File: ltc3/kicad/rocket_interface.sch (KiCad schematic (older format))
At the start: 60 parts, among them IC1 TLP3542, J601 RJ45, K601 RELAY_1C, K602 RELAY_1C, P601 BATT-IN, P602 CONN_01x02, P603 UMBILICAL, Q601 PMV45EN, Q602 PMV45EN, SW601 SPST_switch, U602 CD74HC14, U603 SN65220DBV, U604 741G08

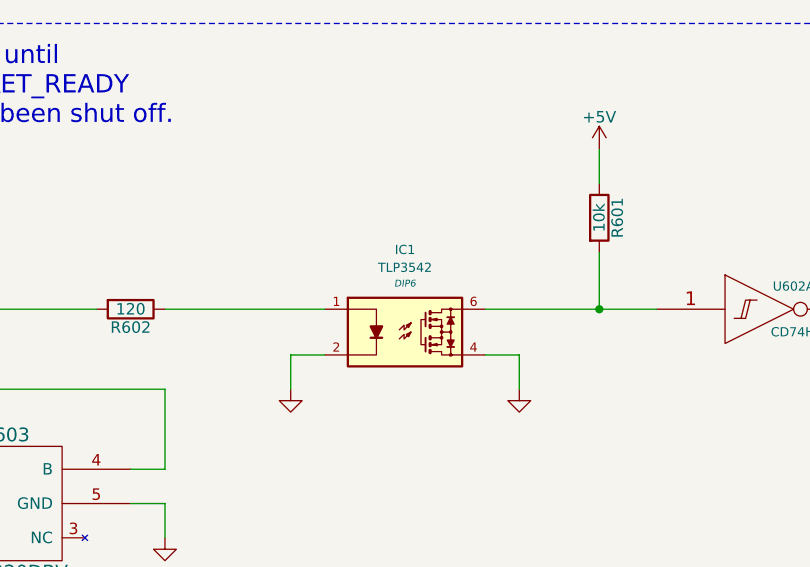
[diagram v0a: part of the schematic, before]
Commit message: Assigned more footprints, created PSOP-6 and PTN78020W.
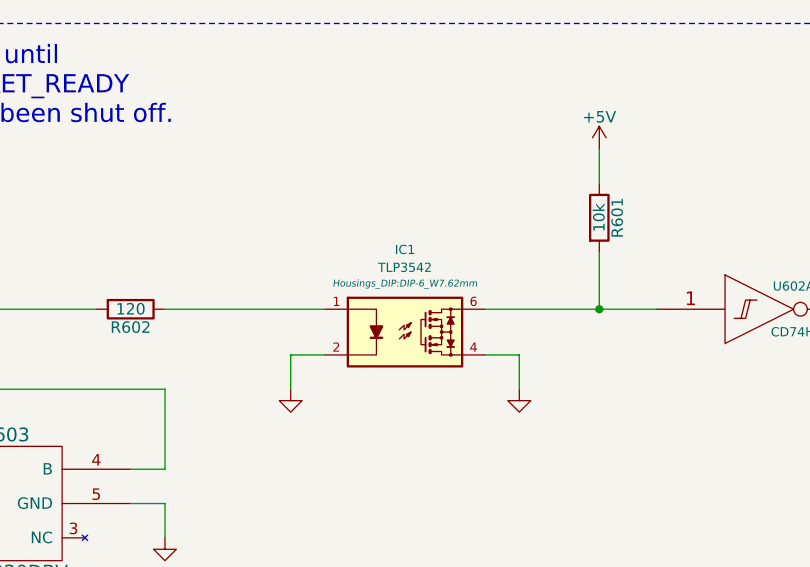
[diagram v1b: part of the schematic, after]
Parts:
- IC1: footprint DIP6 -> Housings_DIP:DIP-6_W7.62mm
- U602: footprint (none) -> Housings_SSOP:TSSOP-14_4.4x5mm_Pitch0.65mm
- U603: footprint (none) -> LTC3:PSOP-6
- U604: footprint (none) -> TO_SOT_Packages_SMD:SOT-353

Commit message: LTC3: Cosmetic changes; reference designator updates; etc.
1. Renamed "PHNTM*" reference designators to something more
   conventional and descriptive (e.g., "PHNTM*" to "BT*" for off-board
   batteries).
2. Cosmetic changes to battery management and BeagleBone schematics
   (normalizing text notes style, etc.).
3. Incremental progress on footprint assignment.
4. Imported netlist into PCB layout editor, just for grins.
   Everything fits into a 250x135mm board.  Only $260 for an OSH Park run!
   There may be some opportunities for improvement...
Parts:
- SW601: footprint (none) -> Oddities:Dummy_Empty
- W20, W21, W22, W23, W24, W25, W26, W27: footprint (none) -> Measurement_Points:Test_Point_2Pads
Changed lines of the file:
@@
 F 0 "SW601" H 14350 7050 60  0000 C CNN
 F 1 "SPST_switch" H 14370 6830 60  0001 C CNN
-F 2 "" H 14370 6950 60  0001 C CNN
+F 2 "Oddities:Dummy_Empty" H 14370 6950 60  0001 C CNN
 F 3 "" H 14370 6950 60  0000 C CNN
 F 4 "Ign. Arm" H 14350 6800 60  0000 C CNN "Note"
@@
 F 0 "W20" V 1404 2408 50  0000 L CNN
 F 1 "0/5V" V 1496 2408 50  0000 L CNN
-F 2 "" H 1450 2350 50  0001 C CNN
+F 2 "Measurement_Points:Test_Point_2Pads" H 1450 2350 50  0001 C CNN
 F 3 "" H 1450 2350 50  0000 C CNN
 	1    1450 2350
@@
 F 0 "W26" H 14750 1400 50  0000 C CNN
 F 1 "14.8-16.8V" H 14750 1500 50  0000 C CNN
-F 2 "" H 14750 1300 50  0001 C CNN
+F 2 "Measurement_Points:Test_Point_2Pads" H 14750 1300 50  0001 C CNN
 F 3 "" H 14750 1300 50  0000 C CNN
 	1    14750 1300
@@
 F 0 "W22" V 7350 3950 50  0000 L CNN
 F 1 "0/5V" V 7450 3850 50  0000 L CNN
-F 2 "" H 7400 4100 50  0001 C CNN
+F 2 "Measurement_Points:Test_Point_2Pads" H 7400 4100 50  0001 C CNN
 F 3 "" H 7400 4100 50  0000 C CNN
 	1    7400 4100
@@
 F 0 "W23" V 7504 4158 50  0000 L CNN
 F 1 "0/5V" V 7596 4158 50  0000 L CNN
-F 2 "" H 7550 4100 50  0001 C CNN
+F 2 "Measurement_Points:Test_Point_2Pads" H 7550 4100 50  0001 C CNN
 F 3 "" H 7550 4100 50  0000 C CNN
 	1    7550 4100
@@
 F 0 "W25" V 11150 3900 50  0000 L CNN
 F 1 "0/5V" V 11250 3850 50  0000 L CNN
-F 2 "" H 11200 4100 50  0001 C CNN
+F 2 "Measurement_Points:Test_Point_2Pads" H 11200 4100 50  0001 C CNN
 F 3 "" H 11200 4100 50  0000 C CNN
 	1    11200 4100
@@
 F 0 "W24" V 10354 8258 50  0000 L CNN
 F 1 "0/3.3V" V 10446 8258 50  0000 L CNN
-F 2 "" H 10400 8200 50  0001 C CNN
+F 2 "Measurement_Points:Test_Point_2Pads" H 10400 8200 50  0001 C CNN
 F 3 "" H 10400 8200 50  0000 C CNN
 	1    10400 8200
@@
 F 0 "W21" V 3104 4058 50  0000 L CNN
 F 1 "0/5V" V 3196 4058 50  0000 L CNN
-F 2 "" H 3150 4000 50  0001 C CNN
+F 2 "Measurement_Points:Test_Point_2Pads" H 3150 4000 50  0001 C CNN
 F 3 "" H 3150 4000 50  0000 C CNN
 	1    3150 4000
@@
 F 0 "W27" V 15004 8358 50  0000 L CNN
 F 1 "0/14.8-16.8V" V 15096 8358 50  0000 L CNN
-F 2 "" H 15050 8300 50  0001 C CNN
+F 2 "Measurement_Points:Test_Point_2Pads" H 15050 8300 50  0001 C CNN
 F 3 "" H 15050 8300 50  0000 C CNN
 	1    15050 8300

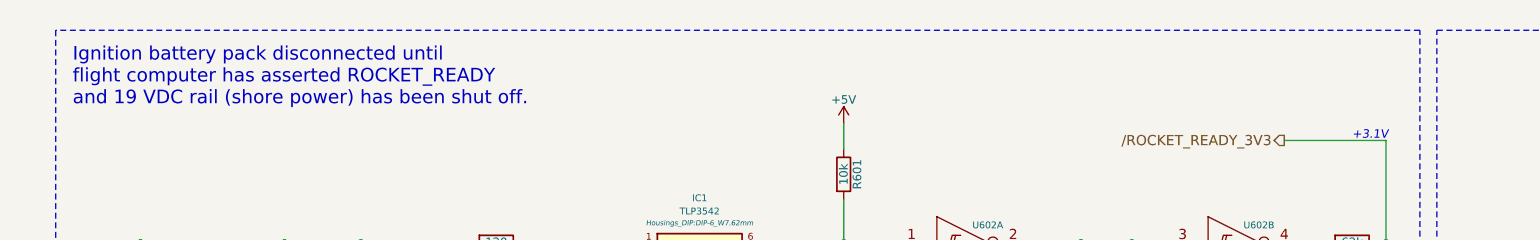
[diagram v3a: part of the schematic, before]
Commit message: Minor adjustment to BB cape footprint; more footprint assignments.
NB: "Valve" footprints are placeholder for components not yet
assigned.
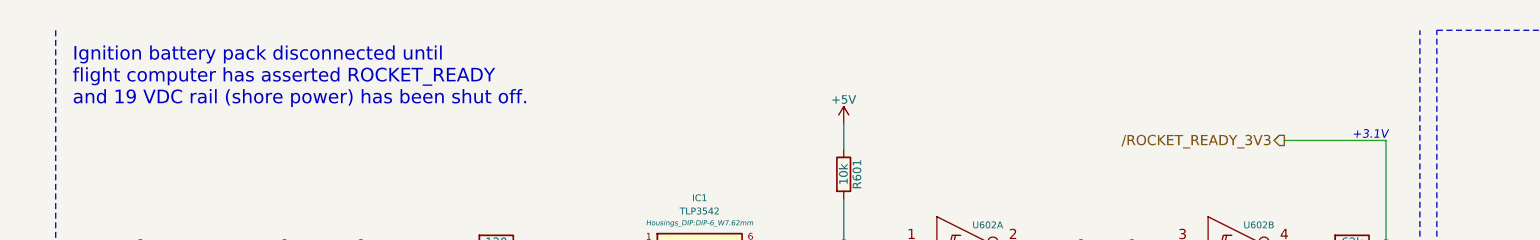
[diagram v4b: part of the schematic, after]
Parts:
- P601, P602: footprint Pin_Headers:Pin_Header_Straight_1x02 -> Valves:VALVE-OCTAL
- P603: footprint Pin_Headers:Pin_Header_Straight_1x10 -> Valves:VALVE-OCTAL
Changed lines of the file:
@@
 F 0 "P602" H 15500 7150 50  0000 C CNN
 F 1 "CONN_01x02" V 15700 7000 50  0000 C CNN
-F 2 "Pin_Headers:Pin_Header_Straight_1x02" H 15600 7000 60  0001 C CNN
+F 2 "Valves:VALVE-OCTAL" H 15600 7000 60  0001 C CNN
 F 3 "" H 15600 7000 60  0000 C CNN
 F 4 "To Away Box" V 15800 7000 60  0000 C CNN "Note"
@@
 F 0 "P601" H 15600 1300 50  0000 C CNN
 F 1 "BATT-IN" V 15700 1150 50  0000 C CNN
-F 2 "Pin_Headers:Pin_Header_Straight_1x02" H 15600 1150 60  0001 C CNN
+F 2 "Valves:VALVE-OCTAL" H 15600 1150 60  0001 C CNN
 F 3 "" H 15600 1150 60  0000 C CNN
 	1    15600 1150
@@
 F 0 "P603" H 1350 7800 50  0000 C CNN
 F 1 "UMBILICAL" V 1450 7250 50  0000 C CNN
-F 2 "Pin_Headers:Pin_Header_Straight_1x10" H 1350 7250 60  0001 C CNN
+F 2 "Valves:VALVE-OCTAL" H 1350 7250 60  0001 C CNN
 F 3 "" H 1350 7250 60  0000 C CNN
 	1    1350 7250
@@
 Wire Notes Line
 	950  4850 9000 4850
-Wire Notes Line
-	9000 800  950  800
 Wire Wire Line
 	9950 2900 11450 2900

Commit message: LTC3: Progress on component value validation, footprint assignment.
1. Added datasheets for large-valued capacitors (Panasonic),
   high-current connectors (Molex MicroFit), etc.
2. Added footprint for BeagleBone Black cape connector.
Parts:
- removed JP601: jumper, Pin_Headers:Pin_Header_Straight_1x02, symbol JUMPER
- added JP601: Shorting Bar, symbol Jumper_NC_Small
- J601: footprint (none) -> Connect:RJ45_8
- renumbered C1 to C604, C604 to C605, C605 to C606, D1 to D609, IC1 to IC601, R606 to R605, R605 to R606, R7 to R614, R614 to R615, R5 to R616, R615 to R617, R616 to R618, R617 to R619, R618 to R620, R4 to R621, R6 to R622, U602 to U601, U603 to U602, U604 to U603, W26 to W601, W20 to W602, W21 to W603, W22 to W604, W23 to W605, W25 to W606, W24 to W607, W27 to W608
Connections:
- net GND_IGN: now also JP601.2
- net at P602.1 (P1), R620.2, SW601.2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: now also JP601.1
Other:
- note added: "TODO: replace jumper w/ conn to\nfront panel shorting bar outlet\n(banana plugs?)"

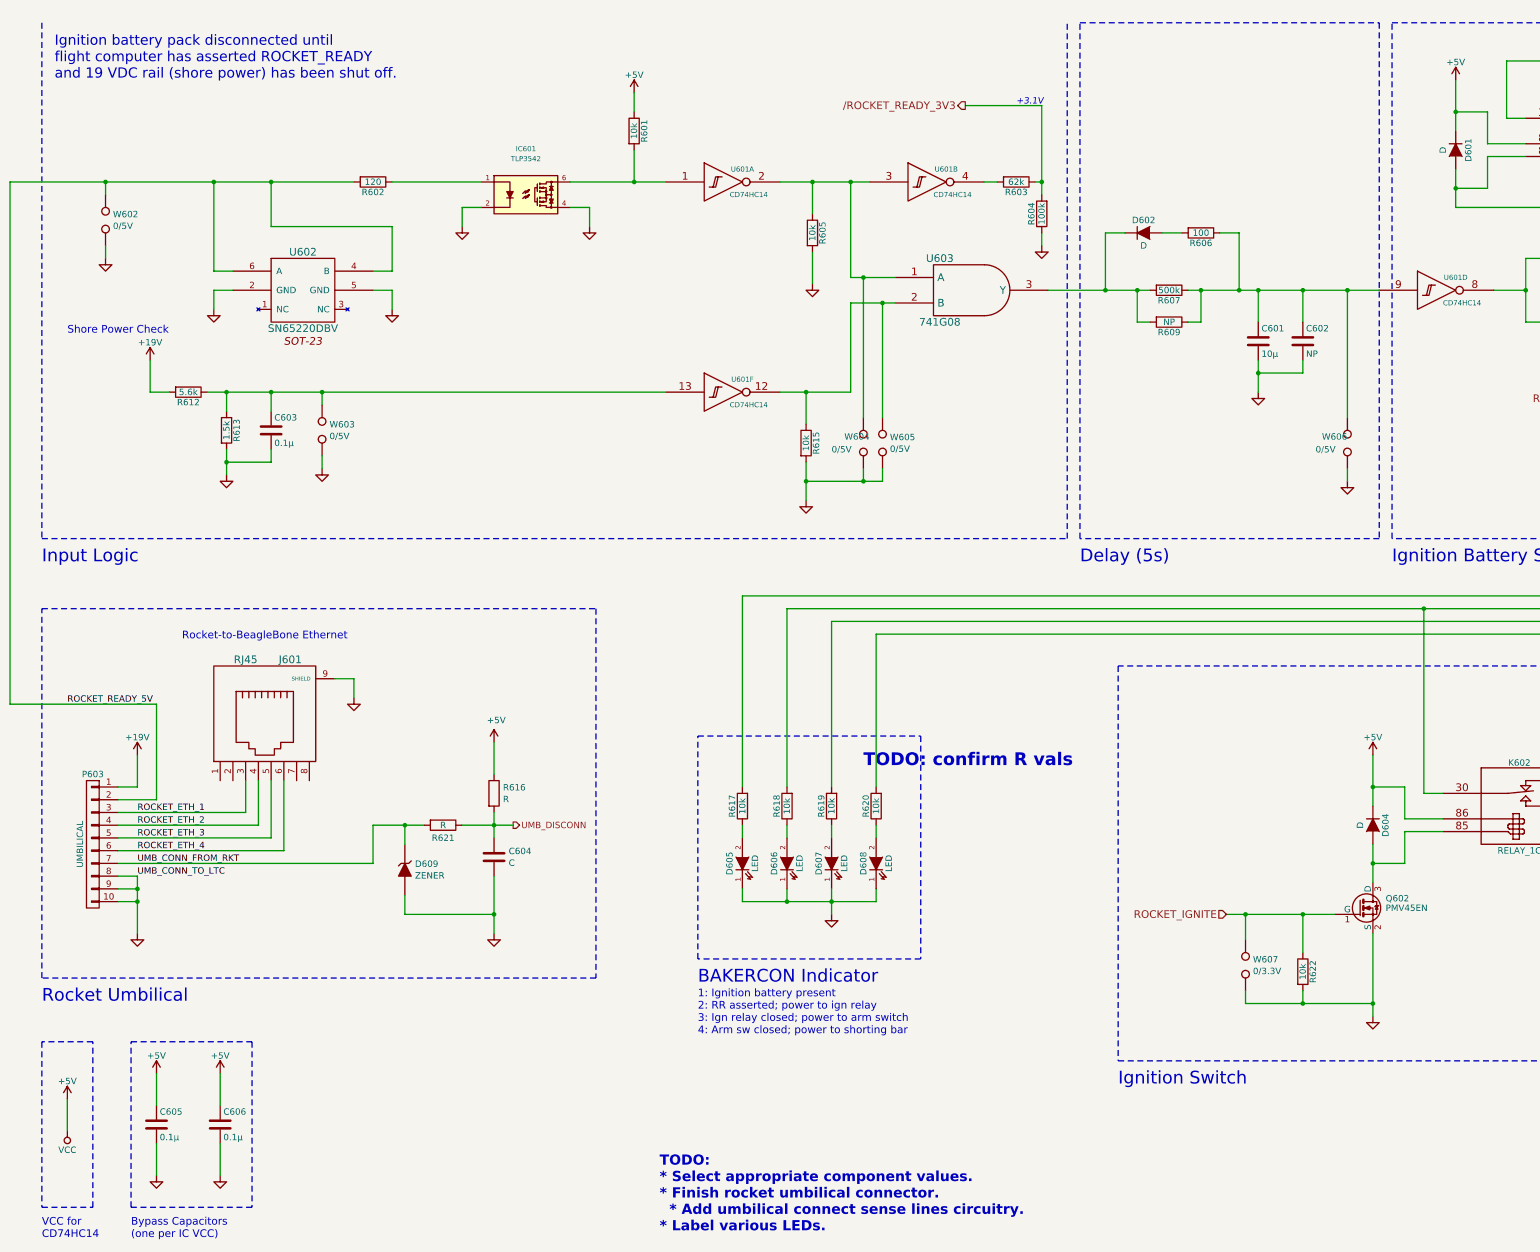
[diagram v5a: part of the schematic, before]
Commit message: LTC3: More component values and footprint assignments.
Split the two-in-one Beagle Bone expansion header component into two
separate components.  Otherwise, we'd be stuck with having to use a
single footprint for the BB cape pin headers, which means pin
numbering that doesn't match the BB docs.
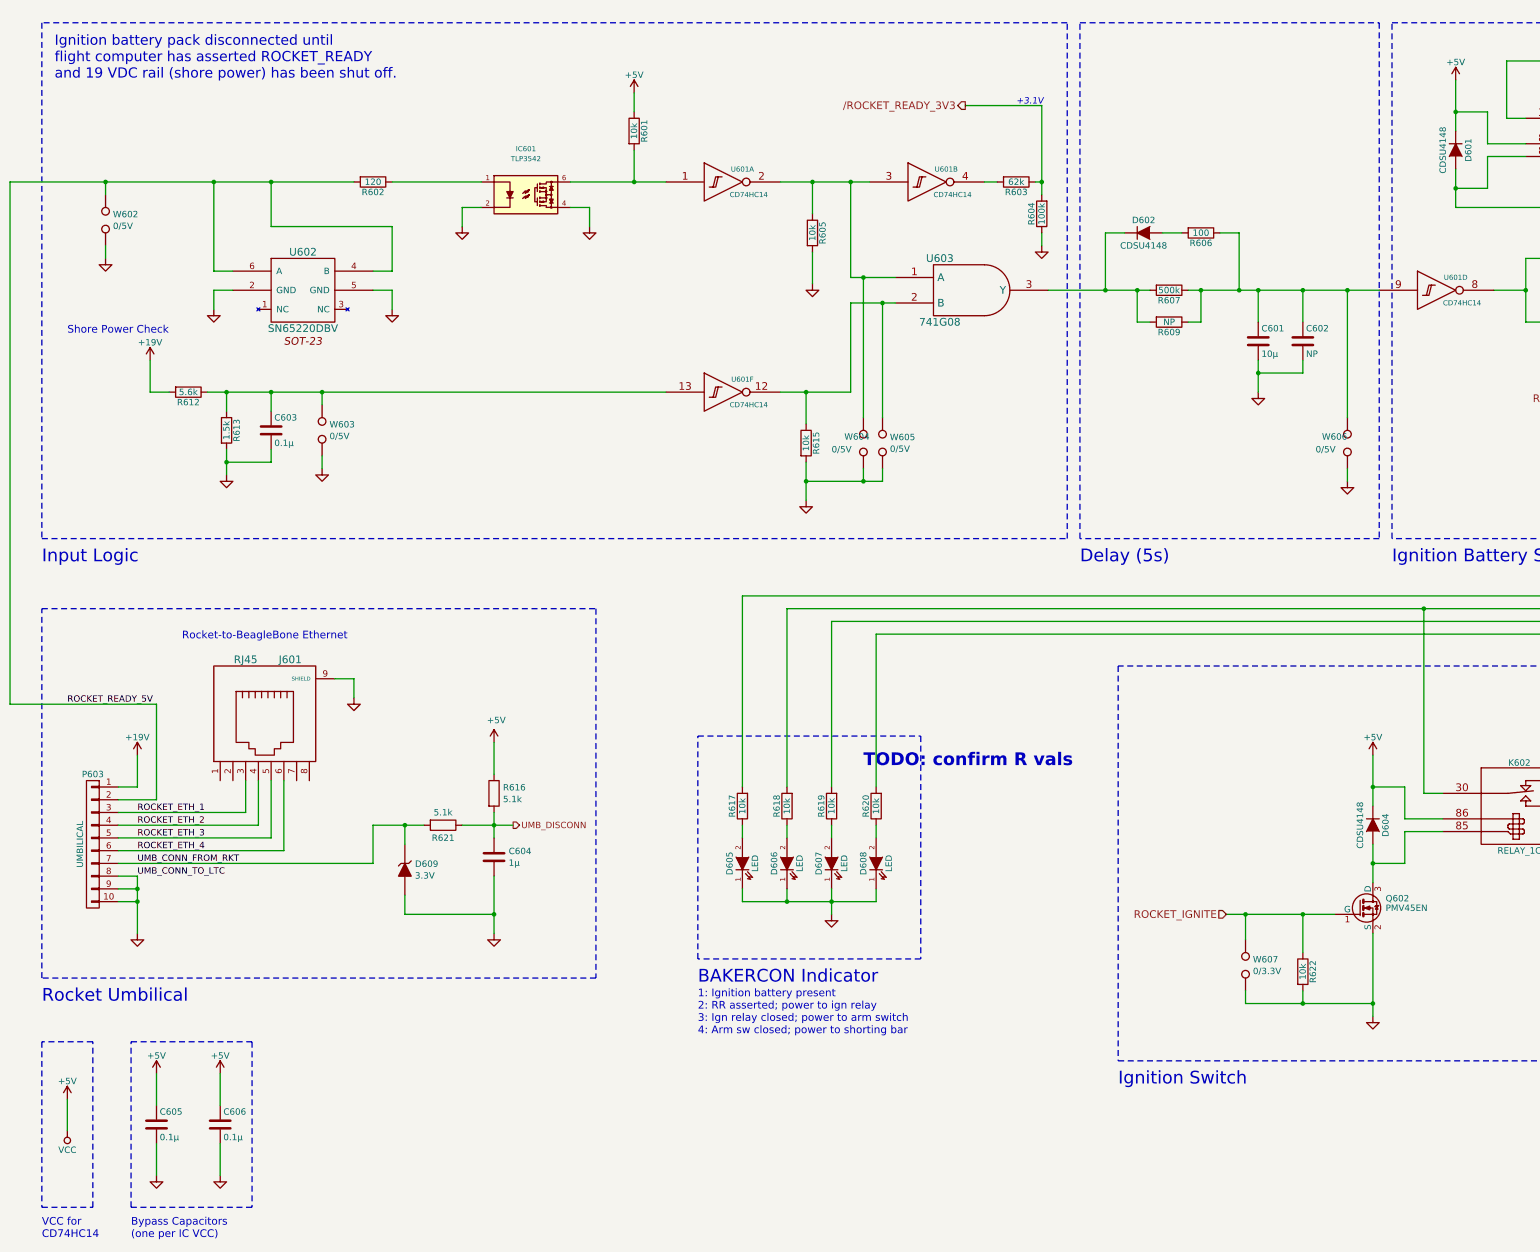
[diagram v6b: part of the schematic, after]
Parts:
- C604: value C -> 1μ
- D601, D602, D604: value D -> CDSU4148; footprint (none) -> Resistors_SMD:R_0603
- D609: value ZENER -> 3.3V; footprint (none) -> Diodes_SMD:SMA_Standard
- R616, R621: value R -> 5.1k
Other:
- note removed: "TODO:\n* Select appropriate component values.\n* Finish rocket umbilical connector.\n * Add umbilical connect sense lines circuitry.\n* Label various LEDs."

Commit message: Assigned component footprints.
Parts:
- R616, R621: footprint (none) -> Resistors_SMD:R_0805
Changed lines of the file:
@@
 EESchema Schematic File Version 2
-LIBS:Launch_Tower_Computer_III-rescue
 LIBS:BeagleBone_Black
 LIBS:LT8490
@@
 LIBS:battery_single_cell
 LIBS:breakers
+LIBS:Launch_Tower_Computer_III-cache
 EELAYER 25 0
 EELAYER END
@@
 F 0 "R621" V 4200 7100 50  0000 C CNN
 F 1 "5.1k" V 4000 7100 50  0000 C CNN
-F 2 "" V 4030 7100 50  0001 C CNN
+F 2 "Resistors_SMD:R_0805" V 4030 7100 50  0001 C CNN
 F 3 "" H 4100 7100 50  0000 C CNN
 	1    4100 7100
@@
 F 0 "R616" H 4570 6896 50  0000 L CNN
 F 1 "5.1k" H 4570 6804 50  0000 L CNN
-F 2 "" V 4430 6850 50  0001 C CNN
+F 2 "Resistors_SMD:R_0805" V 4430 6850 50  0001 C CNN
 F 3 "" H 4500 6850 50  0000 C CNN
 	1    4500 6850

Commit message: LTC3: Created fuse holder footprint; assigned to fuses in schematic.
Created a footprint for Keystone's 3557-2 fuse holder, which accepts a
standard automotive-style ATO/ATC "blade" fuse.  They're cheap,
compact, and plentiful.
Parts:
- F601: footprint (none) -> LTC3:Fuseholder_Auto_Blade_Regular_Keystone_3557-2
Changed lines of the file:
@@
 F 0 "F601" H 13750 7000 50  0000 C CNN
 F 1 "FUSE" H 13550 6900 50  0000 C CNN
-F 2 "" H 13650 6950 60  0001 C CNN
+F 2 "LTC3:Fuseholder_Auto_Blade_Regular_Keystone_3557-2" H 13650 6950 60  0001 C CNN
 F 3 "" H 13650 6950 60  0000 C CNN
 	1    13650 6950
